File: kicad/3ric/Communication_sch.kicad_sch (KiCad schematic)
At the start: 15 parts, among them J1 SNES_Controller_Socket, J2 SNES_Controller_Socket, J3 PS/2 keyboard, J4 Micro_SD_Card

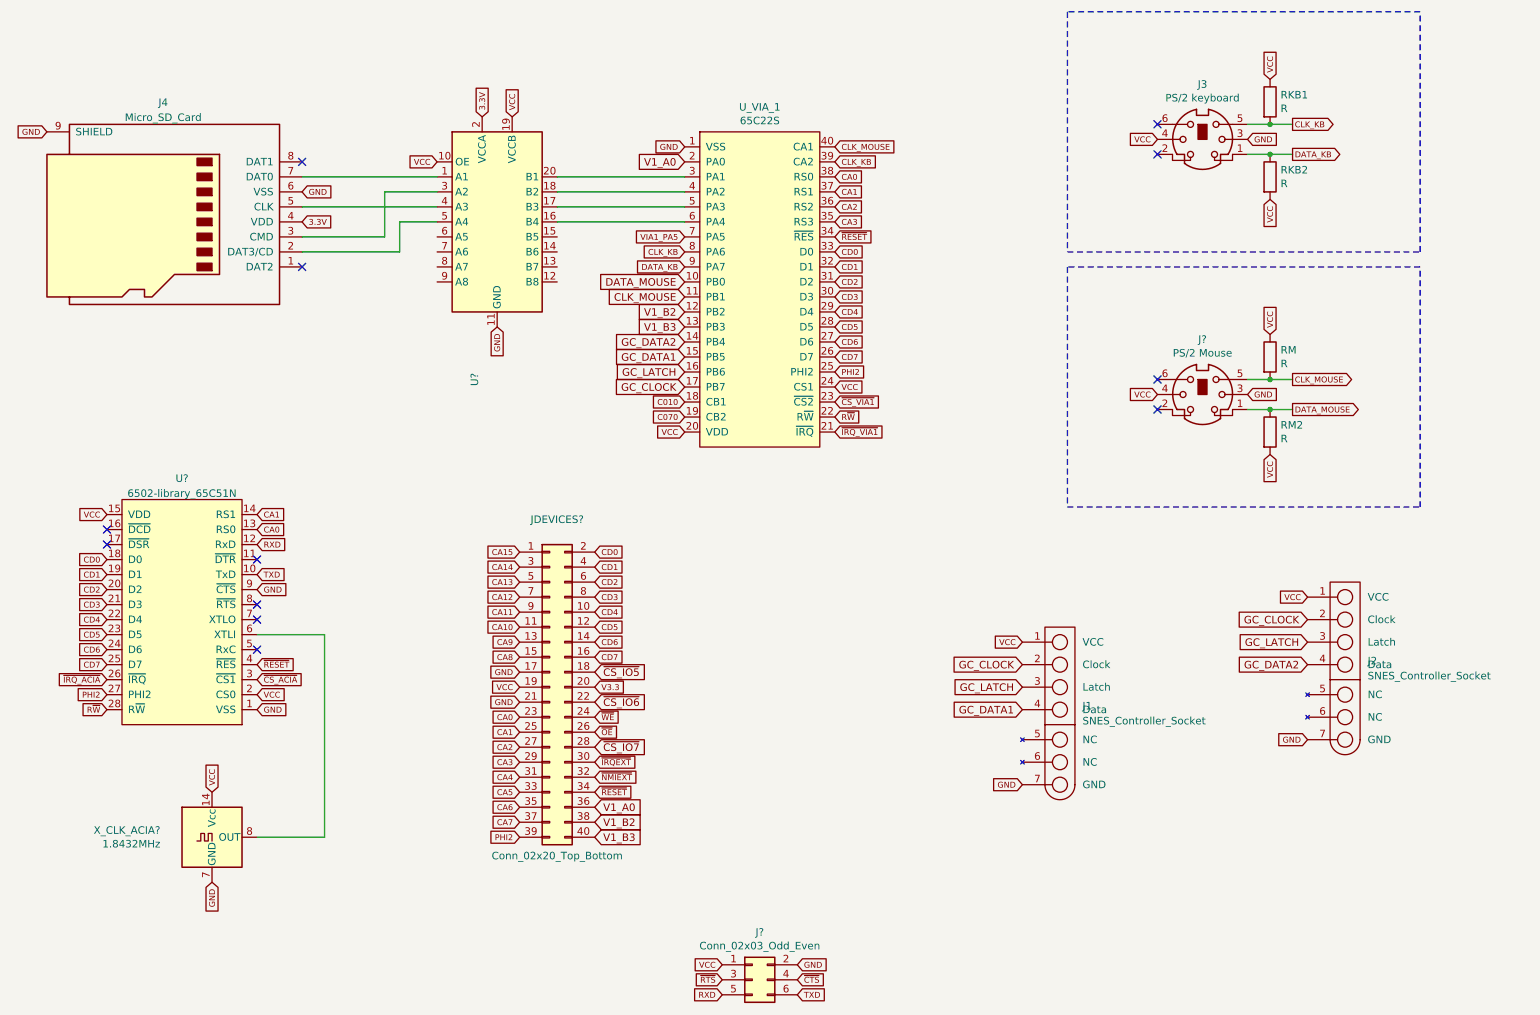
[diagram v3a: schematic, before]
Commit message: update schematic based on breadboard
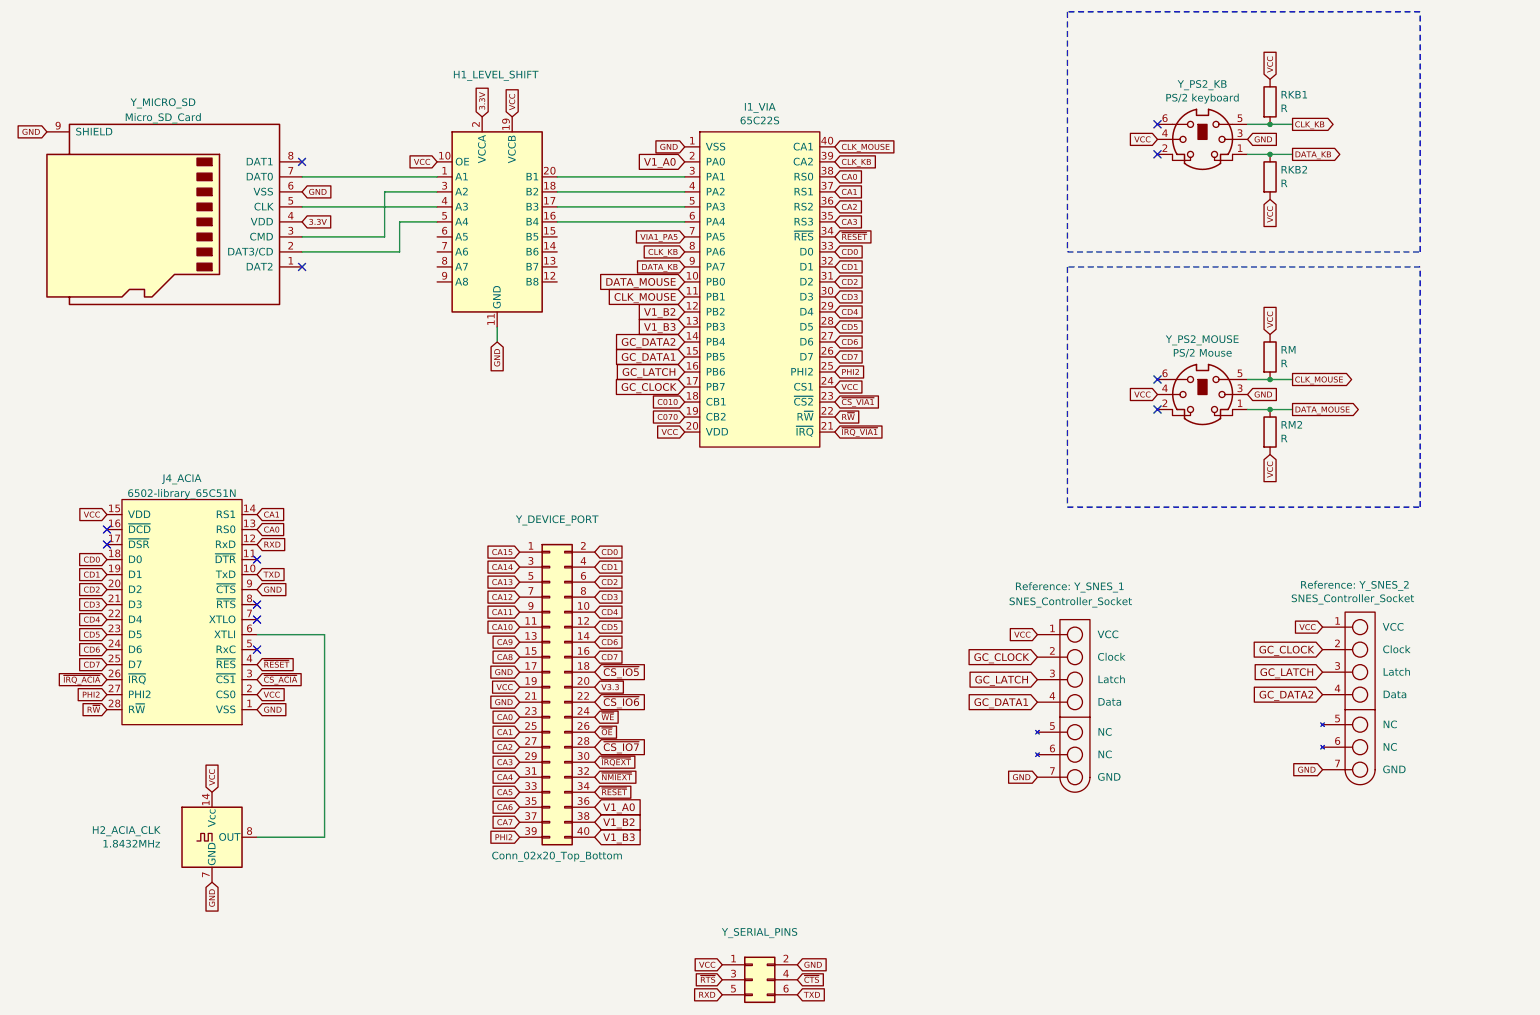
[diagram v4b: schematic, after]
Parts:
- Y_SERIAL_PINS: renamed from J?; value Conn_02x03_Odd_Even -> ~
- gave numbers to parts that had none: 5
- renumbered U_VIA_1 to I1_VIA, J4 to Y_MICRO_SD, J3 to Y_PS2_KB, J1 to Y_SNES_1, J2 to Y_SNES_2
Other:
- moved on the sheet: Reference: Y_SNES_1, Reference: Y_SNES_2
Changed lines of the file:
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@@
 	(wire
 		(pts
+			(xy 107.95 81.28) (xy 107.95 78.74)
+		)
+		(stroke
+			(width 0)
+			(type default)
+		)
+	)
+	(wire
+		(pts
 			(xy 238.76 87.63) (xy 242.57 87.63)
 		)
@@
 	(global_label "GC_CLOCK"
 		(shape input)
-		(at 196.85 135.89 180)
+		(at 199.39 134.62 180)
 		(fields_autoplaced yes)
 		(effects
@@
 		)
 		(property "Intersheetrefs" "${INTERSHEET_REFS}"
-			(at 184.7607 135.8106 0)
+			(at 187.3007 134.5406 0)
 			(effects
 				(font
@@
 	(global_label "VCC"
 		(shape input)
-		(at 245.11 124.46 180)
+		(at 247.65 129.54 180)
 		(fields_autoplaced yes)
 		(effects
@@
 		)
 		(property "Intersheetrefs" "${INTERSHEET_REFS}"
-			(at 85.09 1.27 0)
+			(at 87.63 6.35 0)
 			(effects
 				(font
@@
 	(global_label "GC_CLOCK"
 		(shape input)
-		(at 245.11 128.27 180)
+		(at 247.65 133.35 180)
 		(fields_autoplaced yes)
 		(effects
@@
 		)
 		(property "Intersheetrefs" "${INTERSHEET_REFS}"
-			(at 233.0207 128.1906 0)
+			(at 235.5607 133.2706 0)
 			(effects
 				(font
@@
 	(global_label "GC_DATA1"
 		(shape input)
-		(at 196.85 143.51 180)
+		(at 199.39 142.24 180)
 		(fields_autoplaced yes)
 		(effects
@@
 		)
 		(property "Intersheetrefs" "${INTERSHEET_REFS}"
-			(at 185.305 143.4306 0)
+			(at 187.845 142.1606 0)
 			(effects
 				(font
@@
 	(global_label "GC_LATCH"
 		(shape input)
-		(at 245.11 132.08 180)
+		(at 247.65 137.16 180)
 		(fields_autoplaced yes)
 		(effects
@@
 		)
 		(property "Intersheetrefs" "${INTERSHEET_REFS}"
-			(at 233.5045 132.0006 0)
+			(at 236.0445 137.0806 0)
 			(effects
 				(font
@@
 	(global_label "GND"
 		(shape input)
-		(at 107.95 78.74 270)
+		(at 107.95 81.28 270)
 		(fields_autoplaced yes)
 		(effects
@@
 		)
 		(property "Intersheetrefs" "${INTERSHEET_REFS}"
-			(at 33.02 238.76 0)
+			(at 33.02 241.3 0)
 			(effects
 				(font
@@
 	(global_label "GND"
 		(shape input)
-		(at 245.11 148.59 180)
+		(at 247.65 153.67 180)
 		(fields_autoplaced yes)
 		(effects
@@
 		)
 		(property "Intersheetrefs" "${INTERSHEET_REFS}"
-			(at 85.09 223.52 0)
+			(at 87.63 228.6 0)
 			(effects
 				(font
@@
 	(global_label "VCC"
 		(shape input)
-		(at 196.85 132.08 180)
+		(at 199.39 130.81 180)
 		(fields_autoplaced yes)
 		(effects
@@
 		)
 		(property "Intersheetrefs" "${INTERSHEET_REFS}"
-			(at 36.83 8.89 0)
+			(at 39.37 7.62 0)
 			(effects
 				(font
@@
 	(global_label "GC_LATCH"
 		(shape input)
-		(at 196.85 139.7 180)
+		(at 199.39 138.43 180)
 		(fields_autoplaced yes)
 		(effects
@@
 		)
 		(property "Intersheetrefs" "${INTERSHEET_REFS}"
-			(at 185.2445 139.6206 0)
+			(at 187.7845 138.3506 0)
 			(effects
 				(font
@@
 	(global_label "GC_DATA2"
 		(shape input)
-		(at 245.11 135.89 180)
+		(at 247.65 140.97 180)
 		(fields_autoplaced yes)
 		(effects
@@
 		)
 		(property "Intersheetrefs" "${INTERSHEET_REFS}"
-			(at 233.565 135.8106 0)
+			(at 236.105 140.8906 0)
 			(effects
 				(font
@@
 	(global_label "GND"
 		(shape input)
-		(at 196.85 156.21 180)
+		(at 199.39 154.94 180)
 		(fields_autoplaced yes)
 		(effects
@@
 		)
 		(property "Intersheetrefs" "${INTERSHEET_REFS}"
-			(at 36.83 231.14 0)
+			(at 39.37 229.87 0)
 			(effects
 				(font
@@
 		(on_board yes)
 		(dnp no)
-		(property "Reference" "J3"
+		(property "Reference" "Y_PS2_KB"
 			(at 227.33 37.6682 0)
 			(effects
@@
 			(project "3ric"
 				(path "/e63e39d7-6ac0-4ffd-8aa3-1841a4541b55/817a35a7-de63-4412-ae79-57fde5eabc67"
-					(reference "J3")
+					(reference "Y_PS2_KB")
 					(unit 1)
 				)
@@
 		(dnp no)
 		(fields_autoplaced yes)
-		(property "Reference" "J4"
+		(property "Reference" "Y_MICRO_SD"
 			(at 51.435 40.7502 0)
 			(effects
@@
 			(project "3ric"
 				(path "/e63e39d7-6ac0-4ffd-8aa3-1841a4541b55/817a35a7-de63-4412-ae79-57fde5eabc67"
-					(reference "J4")
+					(reference "Y_MICRO_SD")
 					(unit 1)
 				)
@@
 		(on_board yes)
 		(dnp no)
-		(property "Reference" "J?"
+		(property "Reference" "Y_PS2_MOUSE"
 			(at 227.33 80.8482 0)
 			(effects
@@
 			(project "3ric"
 				(path "/e63e39d7-6ac0-4ffd-8aa3-1841a4541b55/817a35a7-de63-4412-ae79-57fde5eabc67"
-					(reference "J?")
+					(reference "Y_PS2_MOUSE")
 					(unit 1)
 				)
@@
 		(on_board yes)
 		(dnp no)
-		(property "Reference" "JDEVICES?"
+		(property "Reference" "Y_DEVICE_PORT"
 			(at 118.11 111.3282 0)
 			(effects
@@
 			(project "3ric"
 				(path "/e63e39d7-6ac0-4ffd-8aa3-1841a4541b55/817a35a7-de63-4412-ae79-57fde5eabc67"
-					(reference "JDEVICES?")
+					(reference "Y_DEVICE_PORT")
 					(unit 1)
 				)
@@
 		(on_board yes)
 		(dnp no)
-		(property "Reference" "X_CLK_ACIA?"
+		(property "Reference" "H2_ACIA_CLK"
 			(at 50.9524 163.9316 0)
 			(effects
@@
 			(project "3ric"
 				(path "/e63e39d7-6ac0-4ffd-8aa3-1841a4541b55/817a35a7-de63-4412-ae79-57fde5eabc67"
-					(reference "X_CLK_ACIA?")
+					(reference "H2_ACIA_CLK")
 					(unit 1)
 				)
@@
 		(on_board yes)
 		(dnp no)
-		(property "Reference" "U_VIA_1"
+		(property "Reference" "I1_VIA"
 			(at 152.4 41.529 0)
 			(effects
@@
 			(project "3ric"
 				(path "/e63e39d7-6ac0-4ffd-8aa3-1841a4541b55/817a35a7-de63-4412-ae79-57fde5eabc67"
-					(reference "U_VIA_1")
+					(reference "I1_VIA")
 					(unit 1)
 				)
@@
 		(on_board yes)
 		(dnp no)
-		(property "Reference" "J?"
+		(property "Reference" "Y_SERIAL_PINS"
 			(at 152.4 181.1782 0)
 			(effects
@@
 			)
 		)
-		(property "Value" "Conn_02x03_Odd_Even"
+		(property "Value" "~"
 			(at 152.4 183.4896 0)
 			(effects
@@
 			(project "3ric"
 				(path "/e63e39d7-6ac0-4ffd-8aa3-1841a4541b55/817a35a7-de63-4412-ae79-57fde5eabc67"
-					(reference "J?")
+					(reference "Y_SERIAL_PINS")
 					(unit 1)
 				)
@@
 		(on_board yes)
 		(dnp no)
-		(property "Reference" "U?"
-			(at 104.14 87.63 90)
+		(property "Reference" "H1_LEVEL_SHIFT"
+			(at 107.696 36.068 0)
 			(effects
 				(font
@@
 			(project "3ric"
 				(path "/e63e39d7-6ac0-4ffd-8aa3-1841a4541b55/817a35a7-de63-4412-ae79-57fde5eabc67"
-					(reference "U?")
+					(reference "H1_LEVEL_SHIFT")
 					(unit 1)
 				)
@@
 	(symbol
 		(lib_id "SNES-port:SNES_Controller_Socket")
-		(at 203.2 144.78 0)
+		(at 205.74 143.51 0)
 		(unit 1)
 		(exclude_from_sim no)
@@
 		(on_board yes)
 		(dnp no)
-		(fields_autoplaced yes)
-		(property "Reference" "J1"
-			(at 207.01 142.875 0)
+		(property "Reference" "Y_SNES_1"
+			(at 195.58 122.682 0)
+			(show_name yes)
 			(effects
 				(font
@@
 		)
 		(property "Value" "SNES_Controller_Socket"
-			(at 207.01 145.415 0)
+			(at 194.564 125.222 0)
 			(effects
 				(font
@@
 		)
 		(property "Footprint" "Nintendo:SNES_Controller_Socket"
-			(at 191.77 143.51 0)
+			(at 194.31 142.24 0)
 			(effects
 				(font
@@
 		)
 		(property "Datasheet" ""
-			(at 191.77 143.51 0)
+			(at 194.31 142.24 0)
 			(effects
 				(font
@@
 		)
 		(property "Description" ""
-			(at 203.2 144.78 0)
+			(at 205.74 143.51 0)
 			(effects
 				(font
@@
 			(project "3ric"
 				(path "/e63e39d7-6ac0-4ffd-8aa3-1841a4541b55/817a35a7-de63-4412-ae79-57fde5eabc67"
-					(reference "J1")
+					(reference "Y_SNES_1")
 					(unit 1)
 				)
@@
 	(symbol
 		(lib_id "SNES-port:SNES_Controller_Socket")
-		(at 251.46 137.16 0)
+		(at 254 142.24 0)
 		(unit 1)
 		(exclude_from_sim no)
@@
 		(on_board yes)
 		(dnp no)
-		(fields_autoplaced yes)
-		(property "Reference" "J2"
-			(at 255.27 135.255 0)
+		(property "Reference" "Y_SNES_2"
+			(at 243.84 122.428 0)
+			(show_name yes)
 			(effects
 				(font
@@
 		)
 		(property "Value" "SNES_Controller_Socket"
-			(at 255.27 137.795 0)
+			(at 242.316 124.714 0)
 			(effects
 				(font
@@
 		)
 		(property "Footprint" "Nintendo:SNES_Controller_Socket"
-			(at 240.03 135.89 0)
+			(at 242.57 140.97 0)
 			(effects
 				(font
@@
 		)
 		(property "Datasheet" ""
-			(at 240.03 135.89 0)
+			(at 242.57 140.97 0)
 			(effects
 				(font
@@
 		)
 		(property "Description" ""
-			(at 251.46 137.16 0)
+			(at 254 142.24 0)
 			(effects
 				(font
@@
 			(project "3ric"
 				(path "/e63e39d7-6ac0-4ffd-8aa3-1841a4541b55/817a35a7-de63-4412-ae79-57fde5eabc67"
-					(reference "J2")
+					(reference "Y_SNES_2")
 					(unit 1)
 				)
@@
 		(dnp no)
 		(fields_autoplaced yes)
-		(property "Reference" "U?"
+		(property "Reference" "J4_ACIA"
 			(at 54.61 104.3772 0)
 			(effects
@@
 			(project "3ric"
 				(path "/e63e39d7-6ac0-4ffd-8aa3-1841a4541b55/817a35a7-de63-4412-ae79-57fde5eabc67"
-					(reference "U?")
+					(reference "J4_ACIA")
 					(unit 1)
 				)

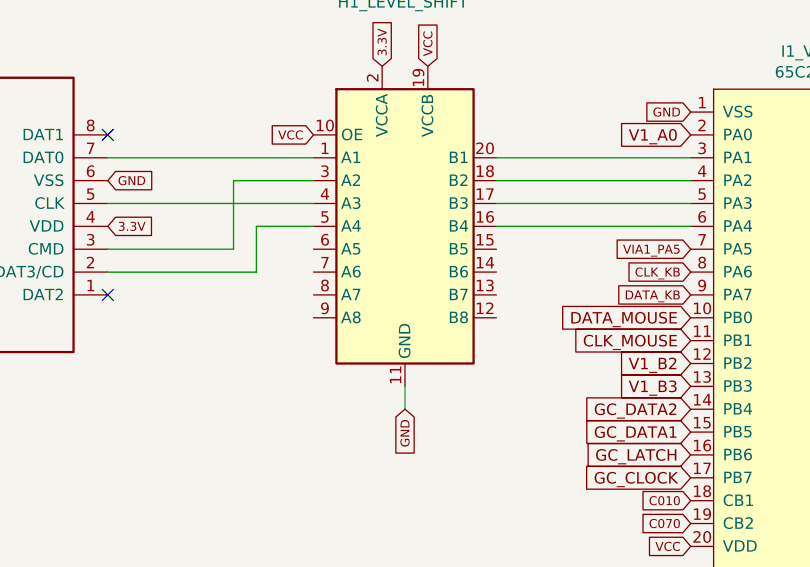
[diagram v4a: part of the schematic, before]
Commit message: completed?  Everything wired in layout creator and first draft of completed schematic
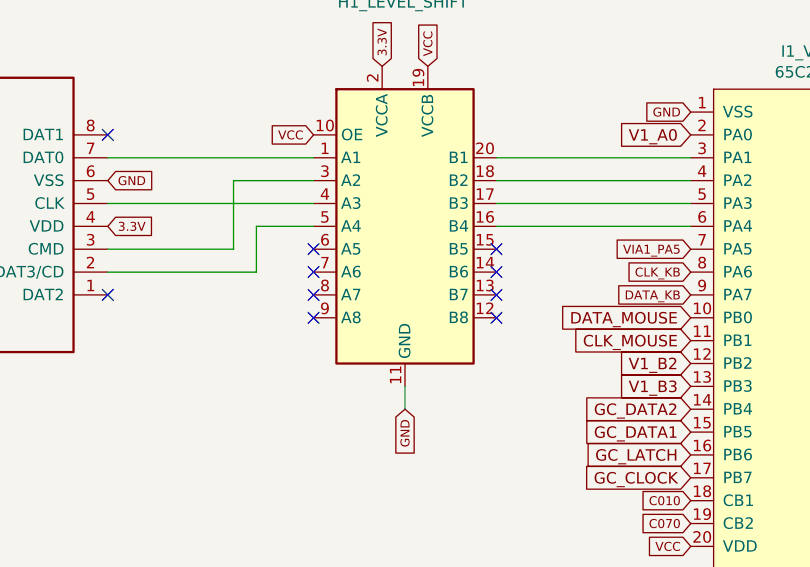
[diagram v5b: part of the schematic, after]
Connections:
- no-connect marks 12 -> 20
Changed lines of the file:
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@@
+	)
+	(no_connect
+		(at 97.79 63.5)
 	)
 	(no_connect
@@
 	)
 	(no_connect
+		(at 97.79 68.58)
+	)
+	(no_connect
 		(at 219.71 49.53)
 	)
@@
 	)
 	(no_connect
+		(at 118.11 68.58)
+	)
+	(no_connect
 		(at 219.71 87.63)
+	)
+	(no_connect
+		(at 97.79 71.12)
 	)
 	(no_connect
@@
 	)
 	(no_connect
+		(at 118.11 71.12)
+	)
+	(no_connect
 		(at 41.91 113.03)
+	)
+	(no_connect
+		(at 118.11 63.5)
 	)
 	(no_connect
 		(at 67.31 128.27)
 	)
+	(no_connect
+		(at 118.11 66.04)
+	)
+	(no_connect
+		(at 97.79 66.04)
+	)
 	(wire
